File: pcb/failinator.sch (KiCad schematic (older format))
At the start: 17 parts, among them P1 CONN_01X04, P2 CONN_01X10, P3 CONN_01X10, U1 MAX7219, U2 RASPIPLUSHEADER

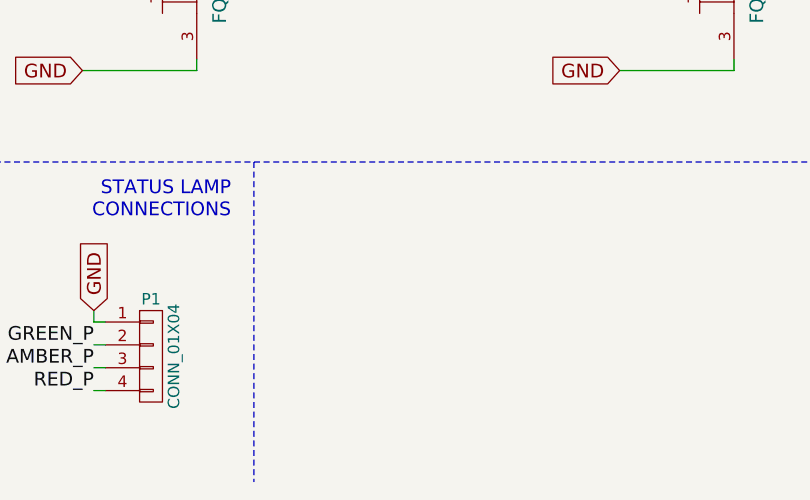
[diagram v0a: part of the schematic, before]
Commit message: Component footprint assignments and netlist.
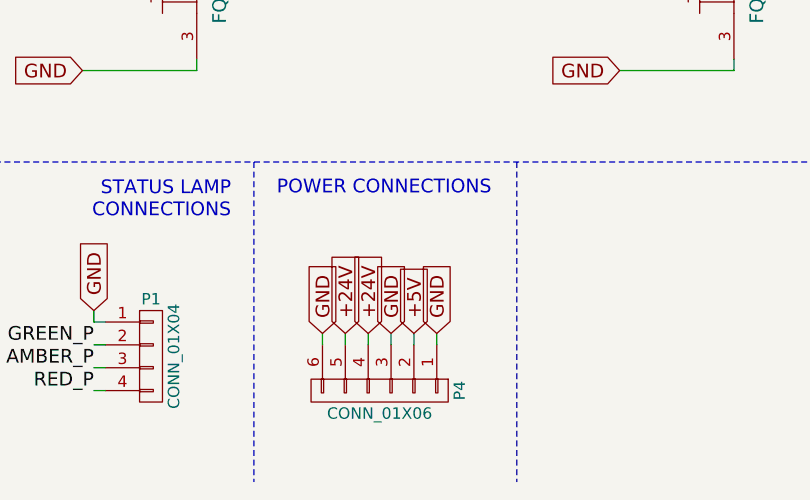
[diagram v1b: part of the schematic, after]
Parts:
- added P4: CONN_01X06, symbol CONN_01X06
- C1: footprint (none) -> failinator:CPOL_2mm
- C2: footprint (none) -> failinator:C_4mm
- MOSFET1, MOSFET2, MOSFET3, MOSFET4, MOSFET5, MOSFET6: footprint (none) -> failinator:TO-251AA
- P2, P3: footprint (none) -> Pin_Headers:Pin_Header_Straight_1x10
- R1, R2, R3, R4: footprint (none) -> Discret:R3
- U1: footprint (none) -> Housings_DIP:DIP-24_W7.62mm_LongPads
- U2: footprint (none) -> Pin_Headers:Pin_Header_Straight_2x20
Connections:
- net +24V: now also P4.4 (P4), P4.5 (P5)
- net +5V: now also P4.2 (P2)
- net GND: now also P4.1 (P1), P4.3 (P3), P4.6 (P6)
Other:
- note added: "POWER CONNECTIONS"
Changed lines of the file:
@@
 F 0 "U2" H 1300 3650 60  0000 C CNN
 F 1 "RASPIPLUSHEADER" H 1750 850 60  0000 C CNN
-F 2 "" H 1700 2050 60  0000 C CNN
+F 2 "Pin_Headers:Pin_Header_Straight_2x20" H 1700 2050 60  0001 C CNN
 F 3 "" H 1700 2050 60  0000 C CNN
 	1    1700 2300
@@
 F 0 "U1" H 8800 2500 60  0000 C CNN
 F 1 "MAX7219" H 9450 700 60  0000 C CNN
-F 2 "" H 9050 2100 60  0000 C CNN
+F 2 "Housings_DIP:DIP-24_W7.62mm_LongPads" H 9050 2100 60  0001 C CNN
 F 3 "" H 9050 2100 60  0000 C CNN
 	1    9200 1600
@@
 F 0 "R4" V 8450 950 50  0000 C CNN
 F 1 "R" V 8350 950 50  0000 C CNN
-F 2 "" V 8280 950 30  0000 C CNN
+F 2 "Discret:R3" V 8280 950 30  0001 C CNN
 F 3 "" H 8350 950 30  0000 C CNN
 	1    8350 950
@@
 F 0 "P2" H 9500 5400 50  0000 C CNN
 F 1 "CONN_01X10" V 9600 4850 50  0000 C CNN
-F 2 "" H 9500 4850 60  0000 C CNN
+F 2 "Pin_Headers:Pin_Header_Straight_1x10" H 9500 4850 60  0001 C CNN
 F 3 "" H 9500 4850 60  0000 C CNN
 	1    9500 4850
@@
 F 0 "P3" H 9500 6550 50  0000 C CNN
 F 1 "CONN_01X10" V 9600 6000 50  0000 C CNN
-F 2 "" H 9500 6000 60  0000 C CNN
+F 2 "Pin_Headers:Pin_Header_Straight_1x10" H 9500 6000 60  0001 C CNN
 F 3 "" H 9500 6000 60  0000 C CNN
 	1    9500 6000
@@
 F 0 "C1" H 9125 3450 50  0000 L CNN
 F 1 "10u" H 9125 3250 50  0000 L CNN
-F 2 "" H 9138 3200 30  0000 C CNN
+F 2 "failinator:CPOL_2mm" H 9138 3200 30  0001 C CNN
 F 3 "" H 9100 3350 60  0000 C CNN
 	1    9100 3350
@@
 F 0 "C2" H 9525 3450 50  0000 L CNN
 F 1 "100n" H 9525 3250 50  0000 L CNN
-F 2 "" H 9538 3200 30  0000 C CNN
+F 2 "failinator:C_4mm" H 9538 3200 30  0001 C CNN
 F 3 "" H 9500 3350 60  0000 C CNN
 	1    9500 3350
@@
 F 0 "P1" H 1600 7650 50  0000 C CNN
 F 1 "CONN_01X04" V 1700 7400 50  0000 C CNN
-F 2 "" H 1600 7400 60  0000 C CNN
+F 2 "" H 1600 7400 60  0001 C CNN
 F 3 "" H 1600 7400 60  0000 C CNN
 	1    1600 7400
@@
 F 0 "MOSFET1" H 1650 6000 60  0000 R CNN
 F 1 "FQU13N06L" V 1900 5700 60  0000 C CNN
-F 2 "" H 1500 5700 60  0000 C CNN
+F 2 "failinator:TO-251AA" H 1500 5700 60  0001 C CNN
 F 3 "" H 1500 5700 60  0000 C CNN
 	1    1500 5700
@@
 F 0 "R1" V 1880 4950 50  0000 C CNN
 F 1 "10k" V 1800 4950 50  0000 C CNN
-F 2 "" V 1730 4950 30  0000 C CNN
+F 2 "Discret:R3" V 1730 4950 30  0001 C CNN
 F 3 "" H 1800 4950 30  0000 C CNN
 	1    1800 4950
@@
 F 0 "MOSFET2" H 2450 5350 60  0000 R CNN
 F 1 "FQU17P06" V 2700 5100 60  0000 C CNN
-F 2 "" H 2300 5050 60  0000 C CNN
+F 2 "failinator:TO-251AA" H 2300 5050 60  0001 C CNN
 F 3 "" H 2300 5050 60  0000 C CNN
 	1    2300 5050
@@
 F 0 "MOSFET3" H 4000 6000 60  0000 R CNN
 F 1 "FQU13N06L" V 4250 5700 60  0000 C CNN
-F 2 "" H 3850 5700 60  0000 C CNN
+F 2 "failinator:TO-251AA" H 3850 5700 60  0001 C CNN
 F 3 "" H 3850 5700 60  0000 C CNN
 	1    3850 5700
@@
 F 0 "R2" V 4230 4950 50  0000 C CNN
 F 1 "10k" V 4150 4950 50  0000 C CNN
-F 2 "" V 4080 4950 30  0000 C CNN
+F 2 "Discret:R3" V 4080 4950 30  0001 C CNN
 F 3 "" H 4150 4950 30  0000 C CNN
 	1    4150 4950
@@
 F 0 "MOSFET4" H 4800 5350 60  0000 R CNN
 F 1 "FQU17P06" V 5050 5100 60  0000 C CNN
-F 2 "" H 4650 5050 60  0000 C CNN
+F 2 "failinator:TO-251AA" H 4650 5050 60  0001 C CNN
 F 3 "" H 4650 5050 60  0000 C CNN
 	1    4650 5050
@@
 F 0 "MOSFET5" H 6450 6000 60  0000 R CNN
 F 1 "FQU13N06L" V 6700 5700 60  0000 C CNN
-F 2 "" H 6300 5700 60  0000 C CNN
+F 2 "failinator:TO-251AA" H 6300 5700 60  0001 C CNN
 F 3 "" H 6300 5700 60  0000 C CNN
 	1    6300 5700
@@
 F 0 "R3" V 6680 4950 50  0000 C CNN
 F 1 "10k" V 6600 4950 50  0000 C CNN
-F 2 "" V 6530 4950 30  0000 C CNN
+F 2 "Discret:R3" V 6530 4950 30  0001 C CNN
 F 3 "" H 6600 4950 30  0000 C CNN
 	1    6600 4950
@@
 F 0 "MOSFET6" H 7250 5350 60  0000 R CNN
 F 1 "FQU17P06" V 7500 5100 60  0000 C CNN
-F 2 "" H 7100 5050 60  0000 C CNN
+F 2 "failinator:TO-251AA" H 7100 5050 60  0001 C CNN
 F 3 "" H 7100 5050 60  0000 C CNN
 	1    7100 5050
@@
 Text Notes 8150 6450 2    60   ~ 0
 STATUS LAMP\nCONTROL
+$Comp
+L CONN_01X06 P4
+U 1 1 56053895
+P 2600 7550
+F 0 "P4" H 2600 7900 50  0000 C CNN
+F 1 "CONN_01X06" V 2700 7550 50  0000 C CNN
+F 2 "" H 2600 7550 60  0000 C CNN
+F 3 "" H 2600 7550 60  0000 C CNN
+	1    2600 7550
+	0    1    1    0
+$EndComp
+Text GLabel 2450 7300 1    60   Input ~ 0
++24V
+Text GLabel 2550 7300 1    60   Input ~ 0
++24V
+Text GLabel 2750 7300 1    60   Input ~ 0
++5V
+Text GLabel 2350 7300 1    60   Input ~ 0
+GND
+Text GLabel 2650 7300 1    60   Input ~ 0
+GND
+Text GLabel 2850 7300 1    60   Input ~ 0
+GND
+Wire Wire Line
+	2350 7300 2350 7350
+Wire Wire Line
+	2450 7300 2450 7350
+Wire Wire Line
+	2550 7300 2550 7350
+Wire Wire Line
+	2650 7300 2650 7350
+Wire Wire Line
+	2750 7300 2750 7350
+Wire Wire Line
+	2850 7300 2850 7350
+Wire Notes Line
+	3200 6550 3200 7950
+Text Notes 2150 6700 0    60   ~ 0
+POWER CONNECTIONS
 $EndSCHEMATC

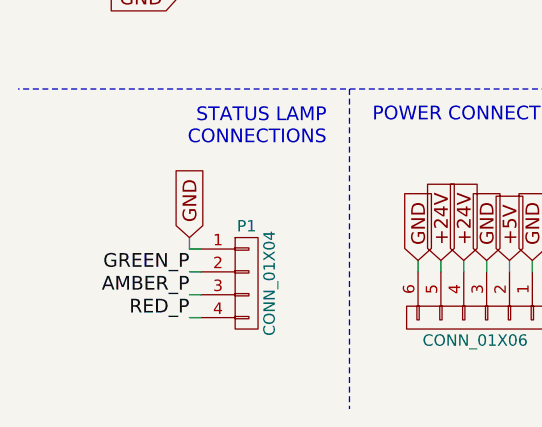
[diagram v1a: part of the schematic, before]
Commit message: Swap the external lamp connections for easier PCB routing.
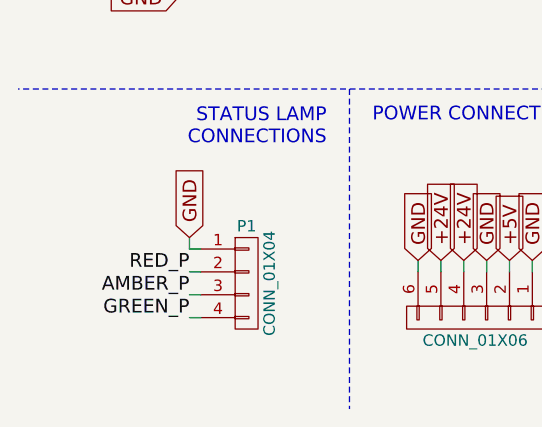
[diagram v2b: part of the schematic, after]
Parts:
- P1: footprint (none) -> failinator:TERM_4
- P4: footprint (none) -> failinator:TERM_6
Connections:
- net GREEN_P: now also P1.4 (P4); no longer P1.2 (P2)
- net RED_P: now also P1.2 (P2); no longer P1.4 (P4)
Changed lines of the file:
@@
 F 0 "P1" H 1600 7650 50  0000 C CNN
 F 1 "CONN_01X04" V 1700 7400 50  0000 C CNN
-F 2 "" H 1600 7400 60  0001 C CNN
+F 2 "failinator:TERM_4" H 1600 7400 60  0001 C CNN
 F 3 "" H 1600 7400 60  0000 C CNN
 	1    1600 7400
 	1    0    0    -1
 $EndComp
-Text Label 1350 7550 2    60   ~ 0
+Text Label 1350 7350 2    60   ~ 0
 RED_P
 Text Label 1350 7450 2    60   ~ 0
 AMBER_P
-Text Label 1350 7350 2    60   ~ 0
+Text Label 1350 7550 2    60   ~ 0
 GREEN_P
 Text GLabel 1350 7200 1    60   Input ~ 0
@@
 F 0 "P4" H 2600 7900 50  0000 C CNN
 F 1 "CONN_01X06" V 2700 7550 50  0000 C CNN
-F 2 "" H 2600 7550 60  0000 C CNN
+F 2 "failinator:TERM_6" H 2600 7550 60  0001 C CNN
 F 3 "" H 2600 7550 60  0000 C CNN
 	1    2600 7550

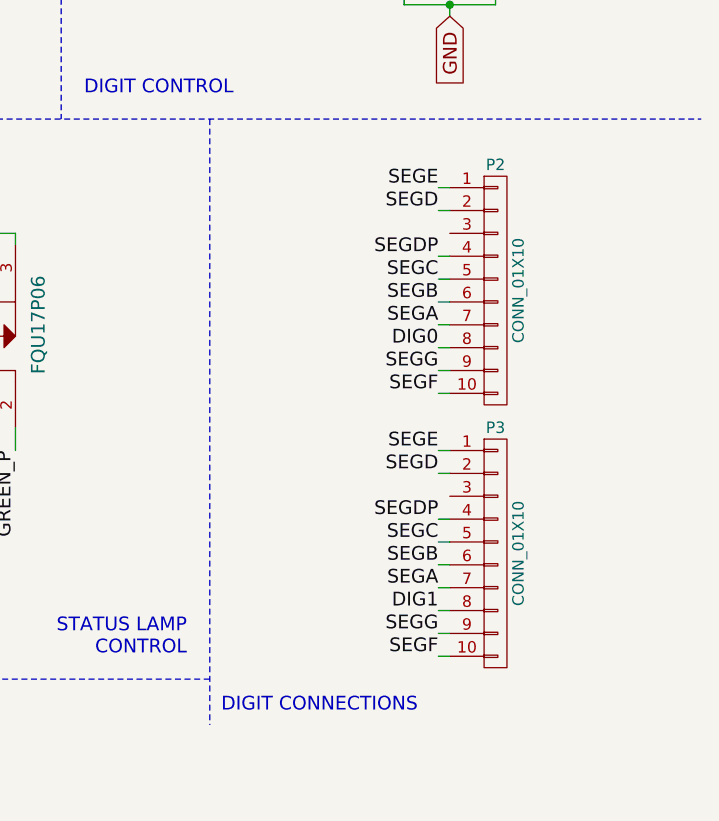
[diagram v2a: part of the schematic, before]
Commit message: Change LED display pinout for a different display.
The other display was too expensive, so switching to a smaller one.
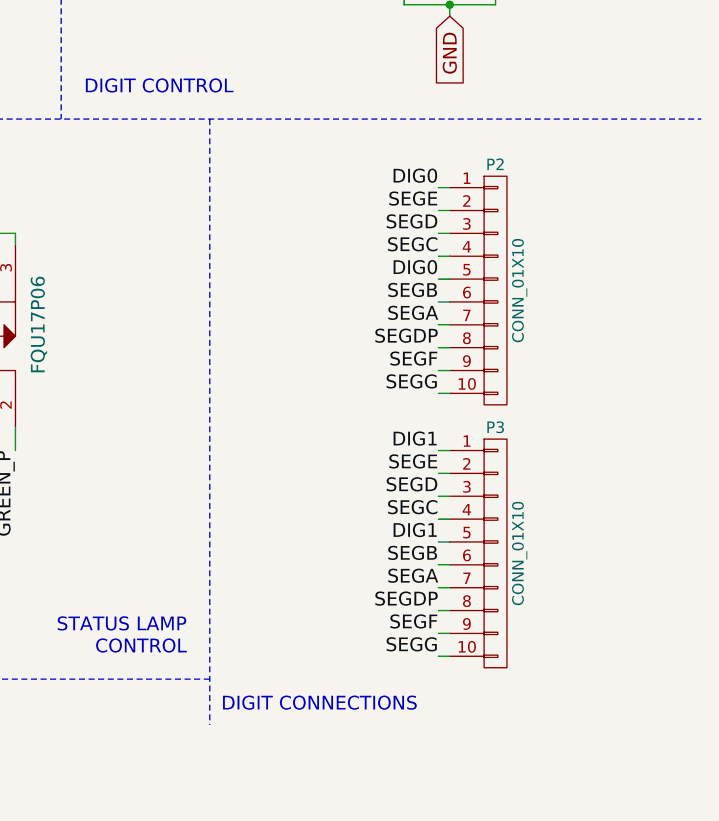
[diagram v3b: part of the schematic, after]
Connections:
- net DIG0: now also P2.1 (P1), P2.5 (P5); no longer P2.8 (P8)
- net DIG1: now also P3.1 (P1), P3.5 (P5); no longer P3.8 (P8)
- net SEGC: now also P2.4 (P4), P3.4 (P4); no longer P2.5 (P5), P3.5 (P5)
- net SEGD: now also P2.3 (P3), P3.3 (P3); no longer P2.2 (P2), P3.2 (P2)
- net SEGDP: now also P2.8 (P8), P3.8 (P8); no longer P2.4 (P4), P3.4 (P4)
- net SEGE: now also P2.2 (P2), P3.2 (P2); no longer P2.1 (P1), P3.1 (P1)
- net SEGF: now also P2.9 (P9), P3.9 (P9); no longer P2.10 (P10), P3.10 (P10)
- net SEGG: now also P2.10 (P10), P3.10 (P10); no longer P2.9 (P9), P3.9 (P9)
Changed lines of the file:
@@
 Wire Wire Line
 	9850 1750 9900 1750
-Text Label 9250 5100 2    60   ~ 0
+Text Label 9250 4400 2    60   ~ 0
 DIG0
-Text Label 9250 6250 2    60   ~ 0
+Text Label 9250 5550 2    60   ~ 0
 DIG1
 Wire Wire Line
@@
 Wire Wire Line
 	9250 6250 9300 6250
-Text Label 9250 5550 2    60   ~ 0
-SEGE
-Text Label 9250 4400 2    60   ~ 0
+Text Label 9250 5650 2    60   ~ 0
 SEGE
 Text Label 9250 4500 2    60   ~ 0
+SEGE
+Text Label 9250 4600 2    60   ~ 0
 SEGD
-Text Label 9250 5650 2    60   ~ 0
+Text Label 9250 5750 2    60   ~ 0
 SEGD
+Text Label 9250 5100 2    60   ~ 0
+SEGDP
+Text Label 9250 6250 2    60   ~ 0
+SEGDP
 Text Label 9250 4700 2    60   ~ 0
-SEGDP
-Text Label 9250 5850 2    60   ~ 0
-SEGDP
-Text Label 9250 4800 2    60   ~ 0
 SEGC
 Text Label 9250 4900 2    60   ~ 0
@@
 Text Label 9250 5000 2    60   ~ 0
 SEGA
-Text Label 9250 5950 2    60   ~ 0
+Text Label 9250 5850 2    60   ~ 0
 SEGC
 Text Label 9250 6050 2    60   ~ 0
@@
 Text Label 9250 6150 2    60   ~ 0
 SEGA
+Text Label 9250 5300 2    60   ~ 0
+SEGG
 Text Label 9250 5200 2    60   ~ 0
+SEGF
+Text Label 9250 6450 2    60   ~ 0
 SEGG
-Text Label 9250 5300 2    60   ~ 0
-SEGF
 Text Label 9250 6350 2    60   ~ 0
-SEGG
-Text Label 9250 6450 2    60   ~ 0
 SEGF
 Wire Wire Line
@@
 Text Notes 2150 6700 0    60   ~ 0
 POWER CONNECTIONS
+Wire Wire Line
+	9250 4600 9300 4600
+Text Label 9250 4800 2    60   ~ 0
+DIG0
+Wire Wire Line
+	9250 5750 9300 5750
+Text Label 9250 5950 2    60   ~ 0
+DIG1
 $EndSCHEMATC
